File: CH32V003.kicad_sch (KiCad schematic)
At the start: 11 parts, among them J4 WCH Link, J5 Program, U3 CH32V003FxPx, X1 X322525MOB4SI

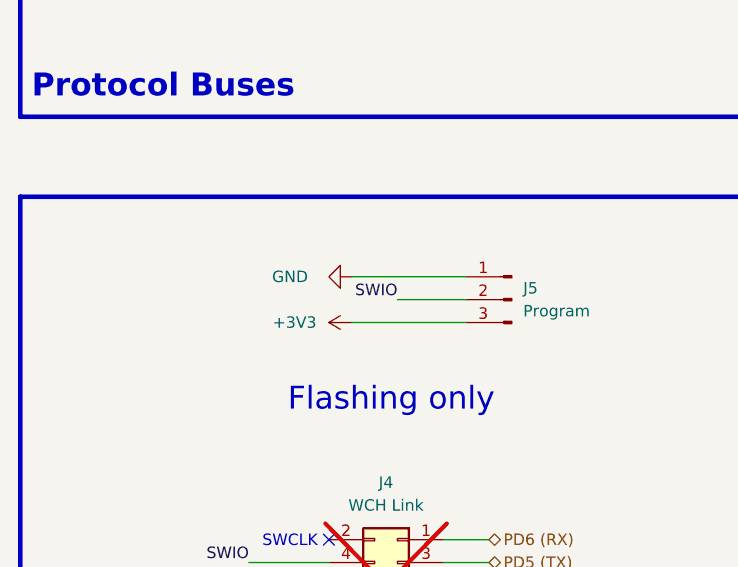
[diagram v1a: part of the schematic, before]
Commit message: BREAKING: updated CH32v003 programming pinout
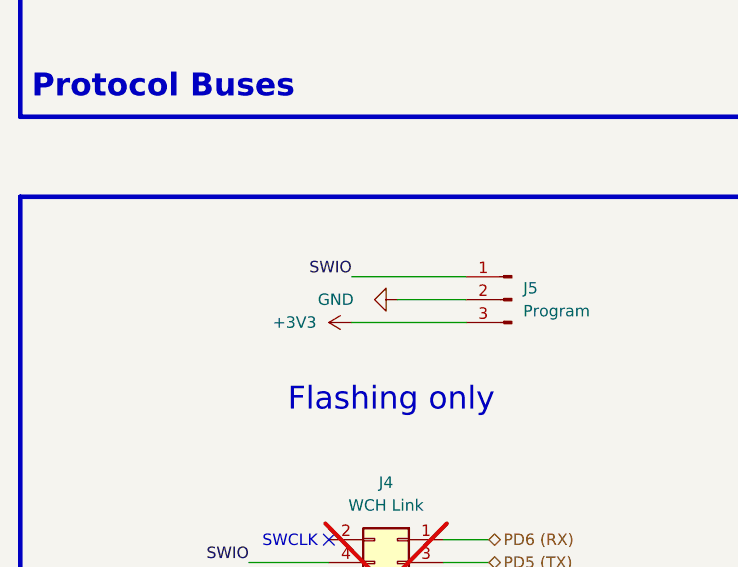
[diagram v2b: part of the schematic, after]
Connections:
- net GND: now also J5.2 (Pin_2); no longer J5.1 (Pin_1)
- net SWIO: now also J5.1 (Pin_1); no longer J5.2 (Pin_2)
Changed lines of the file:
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@@
 	(title_block
 		(title "MMS3 Hat Relay")
-		(rev "A")
+		(date "2026-06-08")
+		(rev "1.1")
 		(company "MiniModucard System")
 		(comment 1 "Wojciech Szafrański")
@@
 	)
 	(label "SWIO"
-		(at 59.69 134.62 180)
+		(at 54.61 132.08 180)
 		(effects
 			(font
@@
 	(symbol
 		(lib_id "power:GND")
-		(at 54.61 132.08 270)
+		(at 59.69 134.62 270)
 		(unit 1)
 		(body_style 1)
@@
 		(dnp no)
 		(property "Reference" "#PWR057"
-			(at 48.26 132.08 0)
+			(at 53.34 134.62 0)
 			(hide yes)
 			(show_name no)
@@
 		)
 		(property "Value" "GND"
-			(at 47.752 132.08 90)
+			(at 52.832 134.62 90)
 			(show_name no)
 			(do_not_autoplace no)
@@
 		)
 		(property "Footprint" ""
-			(at 54.61 132.08 0)
+			(at 59.69 134.62 0)
 			(hide yes)
 			(show_name no)
@@
 		)
 		(property "Datasheet" ""
-			(at 54.61 132.08 0)
+			(at 59.69 134.62 0)
 			(hide yes)
 			(show_name no)
@@
 		)
 		(property "Description" "Power symbol creates a global label with name \"GND\" , ground"
-			(at 54.61 132.08 0)
+			(at 59.69 134.62 0)
 			(hide yes)
 			(show_name no)
